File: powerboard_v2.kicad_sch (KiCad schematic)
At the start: 0 parts

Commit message: 信号制御部の回路図の作成 駆動部への信号は変更する可能性あり
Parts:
- added C1, C10, C2, C3, C4, C5, C6, C7, C9: 0.1uf, symbol Device:C
- added C11, C8: 4.7uf, symbol Device:C
- added D1, D2: D_Shockley, symbol Device:D_Shockley
- added J1, J2, J3: Conn_01x02_Pin, symbol Connector:Conn_01x02_Pin
- added J7: Conn_01x04_Socket, symbol Connector:Conn_01x04_Socket
- added J8: Conn_ST_STDC14, symbol Connector:Conn_ST_STDC14
- added R1: 120, symbol Device:R
- added SW1: SW_Wuerth_450301014042, Button_Switch_THT:SW_Slide-03_Wuerth-WS-SLTV_10x2.5x6.4_P2.54mm, symbol Switch:SW_Wuerth_450301014042
- added SW2: SW_Push, symbol Switch:SW_Push
- added U1: STM32F303K8Tx, Package_QFP:LQFP-32_7x7mm_P0.8mm, symbol MCU_ST_STM32F3:STM32F303K8Tx
- added U2: BD33FC0FP, Package_TO_SOT_SMD:TO-252-2, symbol Regulator_Linear:BD33FC0FP
- added U3: MCP2562-E-P, Package_DIP:DIP-8_W7.62mm, symbol Interface_CAN_LIN:MCP2562-E-P
- added U4: BD50FC0FP, Package_TO_SOT_SMD:TO-252-2, symbol Regulator_Linear:BD50FC0FP
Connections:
- new net: C2.2, U1.1 (VDD)
- new net: C1.2, U1.17 (VDD)
- new net: R1.1, SW1.3 (A)
- new net: C5.1, SW2.2, U1.4 (NRST)
- new net: J1.2 (Pin_2), J2.1 (Pin_1)
- new net +24V: J1.1 (Pin_1)
- new net +3.3V: C1.1, C2.1, C4.1, C6.1, C8.2, D1.2 (A), J8.3 (VCC), U2.3 (VO), U3.5 (Vio)
- new net +5V: C10.1, C11.2, C3.1, D2.2 (A), U3.3 (VDD), U4.3 (VO)
- new net +7.5V: C7.1, C9.1, D1.1 (K), D2.1 (K), J3.1 (Pin_1), J7.1 (Pin_1), U2.1 (VCC), U4.1 (VCC)
- new net GND: C5.2, J2.2 (Pin_2), SW2.1, U1.16 (VSS), U1.32 (VSS)
- new net GND1: C10.2, C11.1, C3.2, C4.2, C6.2, C7.2, C8.1, C9.2, J3.2 (Pin_2), J7.2 (Pin_2), J8.5 (GND), J8.7 (GND), SW1.2 (C), U2.2 (GND), U3.2 (VSS), U3.8 (STBY), U4.2 (GND)
- new net can1_rx: U1.21 (PA11), U3.4 (RXD)
- new net can1_tx: U1.22 (PA12), U3.1 (TXD)
- new net can_h: J7.4 (Pin_4), R1.2, U3.7 (CANH)
- new net can_l: J7.3 (Pin_3), SW1.1 (B), U3.6 (CANL)
- new net output-gnd: J8.11 (GNDDetect)
- new net strx: J8.13 (VCP_RX), U1.26 (PB3)
- new net sttx: J8.14 (VCP_TX), U1.27 (PB4)
- new net swclk: J8.6 (JCLK/SWCLK), U1.24 (PA14)
- new net swdio: J8.4 (JTMS/SWDIO), U1.23 (PA13)
- new net デジタル-駆動間信号: U1.10 (PA4)
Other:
- note added: "マイコン用電源"
- note added: "駆動用電源"

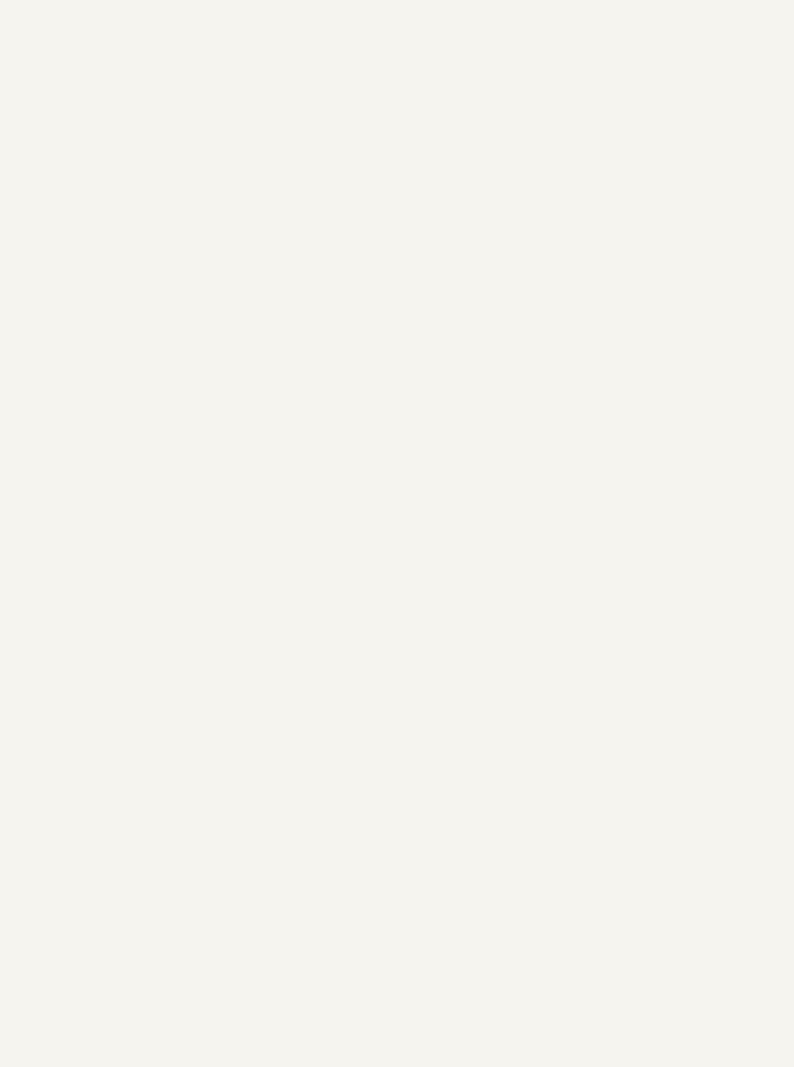
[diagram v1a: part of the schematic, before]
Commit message: リレーの外部ライブラリのインポート
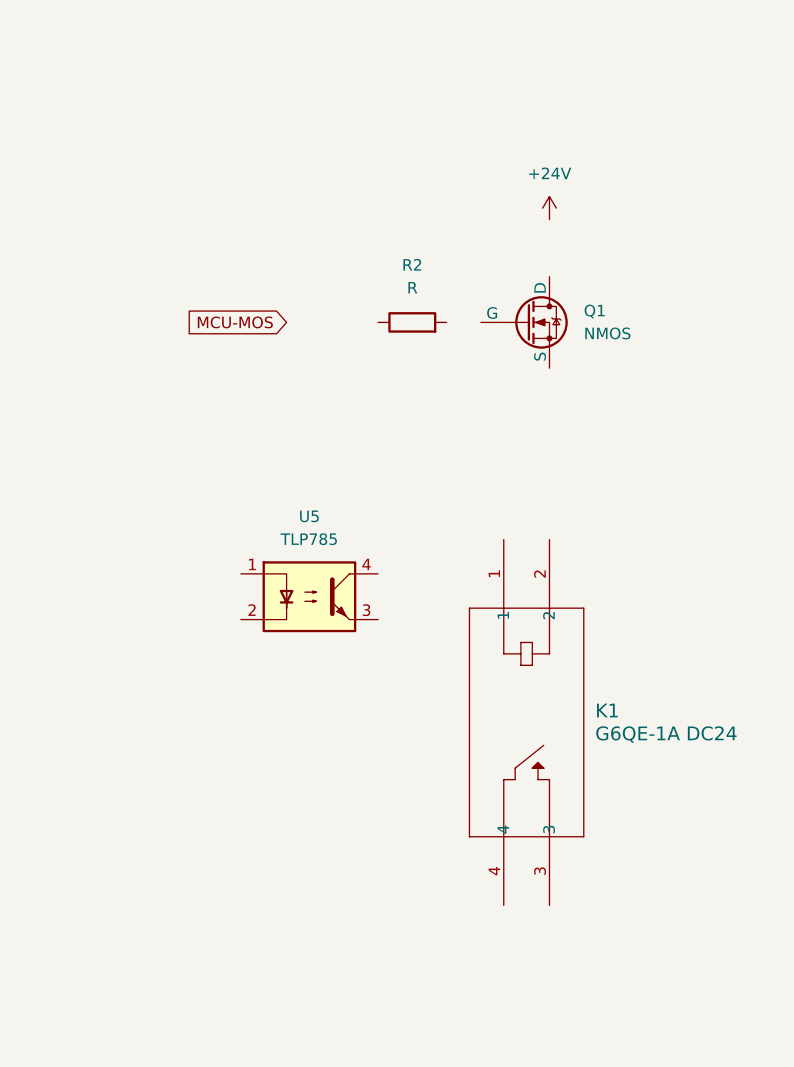
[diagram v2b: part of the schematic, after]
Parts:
- added K1: G6QE-1A DC24, footprints:RELAY_G6QE-1A_OMR, symbol 2026-04-11_13-59-38:G6QE-1A_DC24
- added Q1: NMOS, symbol Simulation_SPICE:NMOS
- added R2: R, symbol Device:R
- added U5: TLP785, Package_DIP:DIP-4_W7.62mm, symbol Isolator:TLP785

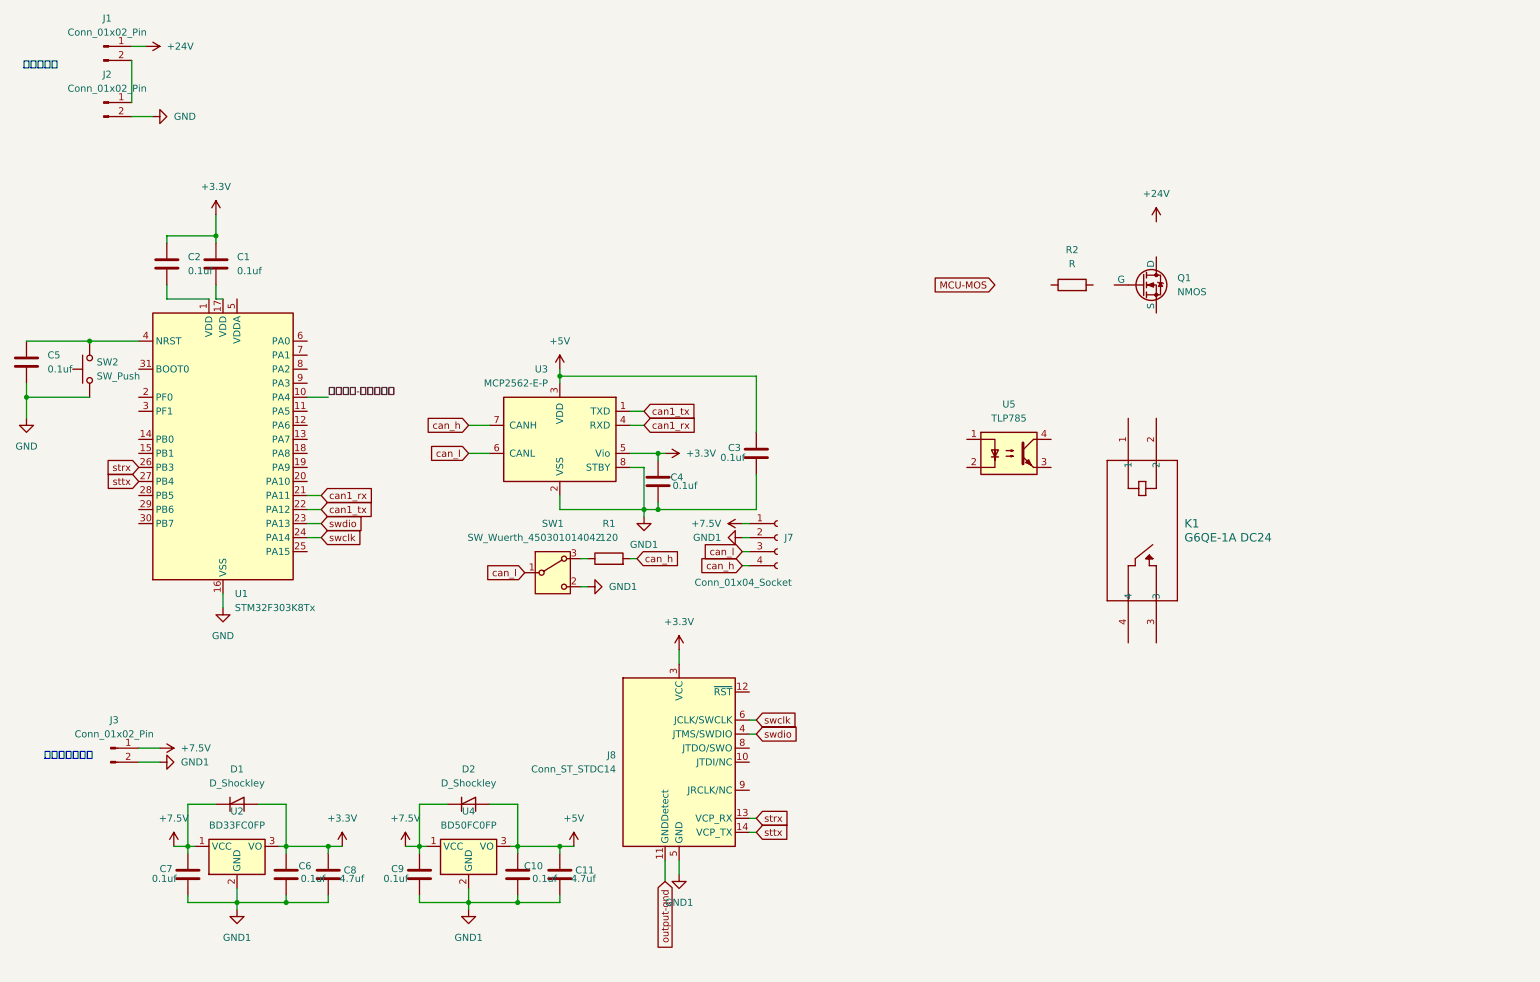
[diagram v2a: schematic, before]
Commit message: 必要部品の配置(フォトカプラ再選定の必要性ありかも？)
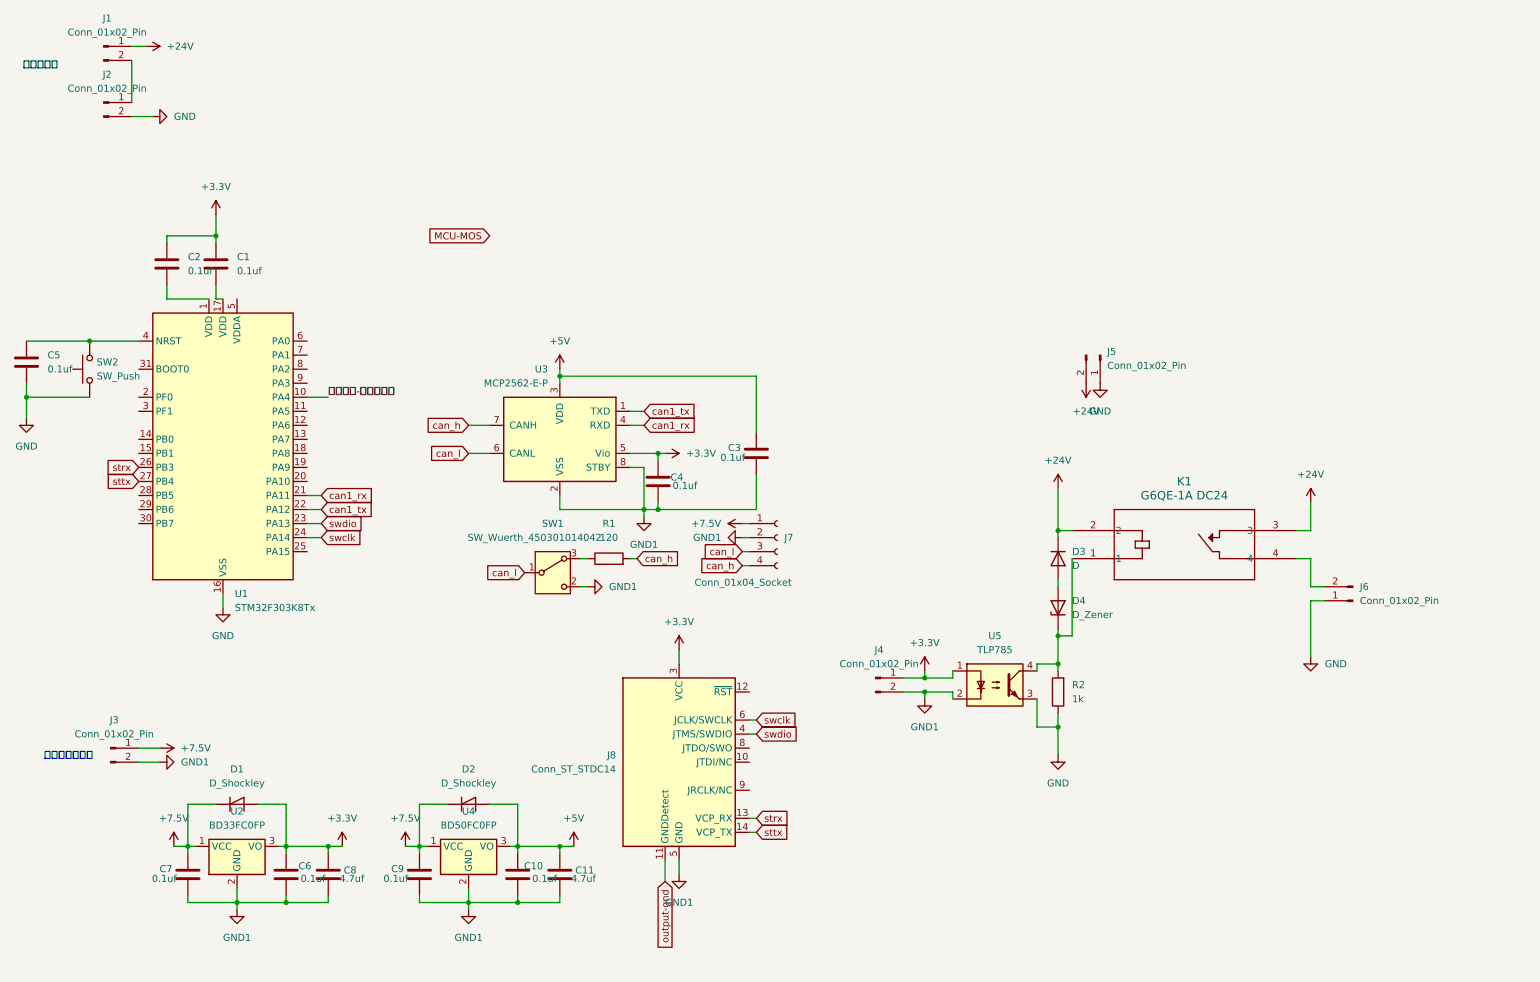
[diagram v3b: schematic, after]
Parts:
- removed Q1: NMOS, symbol Simulation_SPICE:NMOS
- added D3: D, symbol Device:D
- added D4: D_Zener, symbol Device:D_Zener
- added J4, J5, J6: Conn_01x02_Pin, symbol Connector:Conn_01x02_Pin
- R2: value R -> 1k
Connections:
- net +24V: now also K1.2, K1.3, D3.1 (K), J5.2 (Pin_2)
- net +3.3V: now also U5.1, J4.1 (Pin_1)
- net GND: now also R2.1, U5.3, J5.1 (Pin_1), J6.1 (Pin_1)
- net GND1: now also U5.2, J4.2 (Pin_2)
- net at U5.4: now also K1.1, R2.2, D4.1 (K)
- net at K1.4: now also J6.2 (Pin_2)
- new net: D3.2 (A), D4.2 (A)
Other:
- moved on the sheet: K1, R2, U5

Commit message: フォトカプラの置き換えとコンデンサと放電回路の作成(未完了)
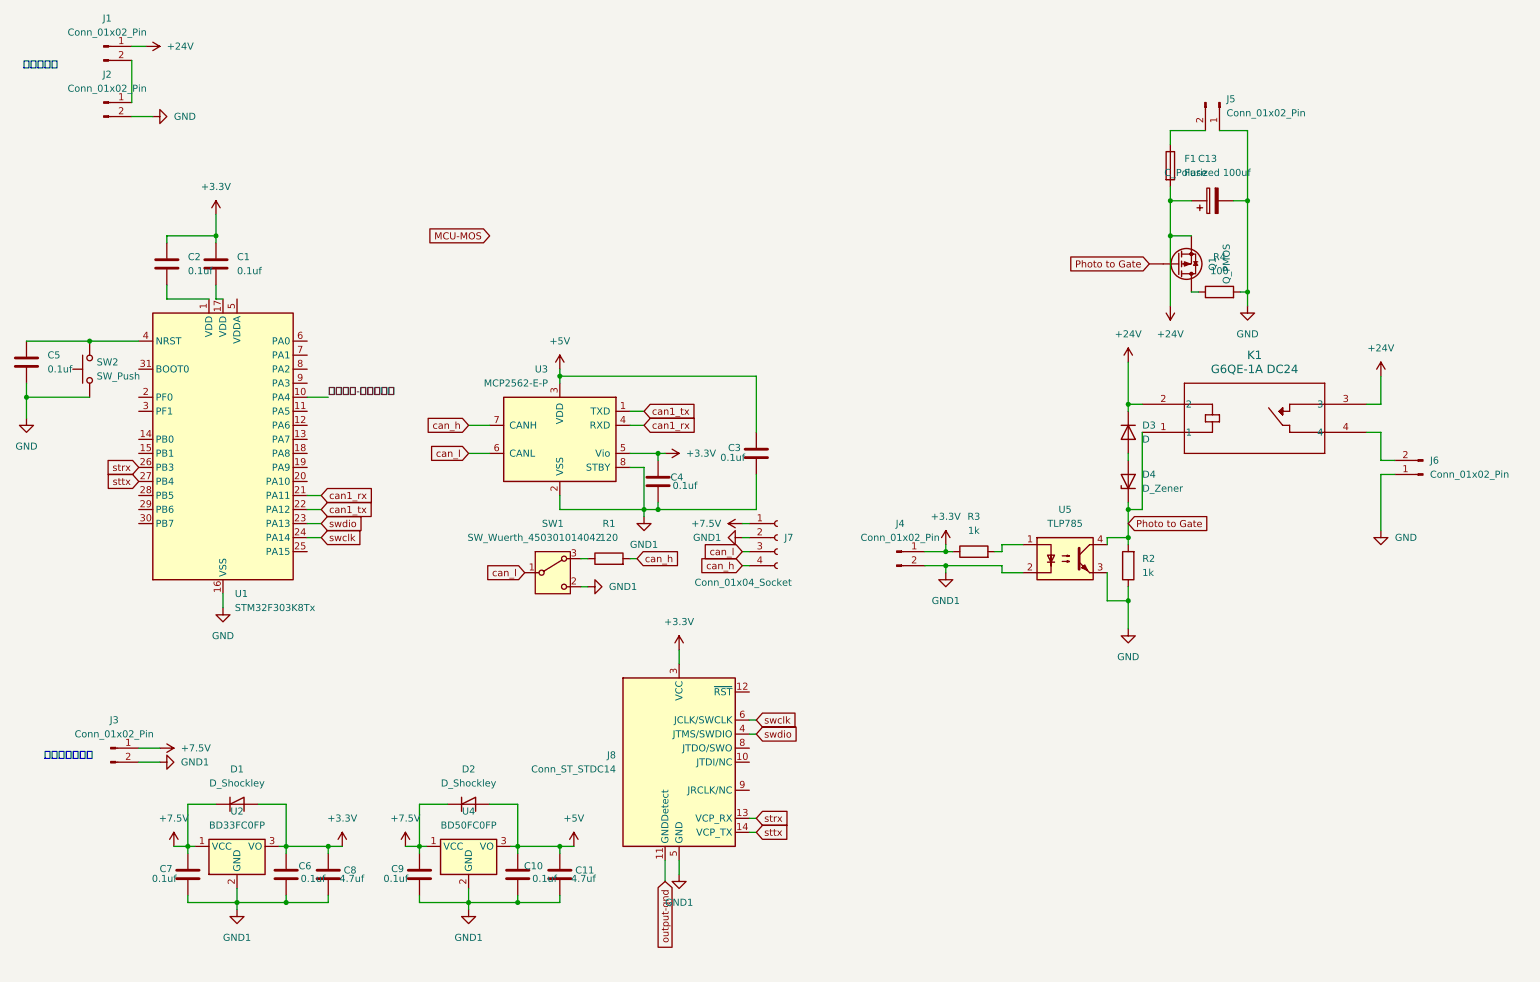
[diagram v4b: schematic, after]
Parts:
- added C13: C_Polarized 100uf, symbol Device:C_Polarized
- added F1: Fuse, symbol Device:Fuse
- added Q1: Q_PMOS, symbol Device:Q_PMOS
- added R3: 1k, symbol Device:R
- added R4: 100, symbol Device:R
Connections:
- net +24V: now also C13.1, F1.2, Q1.S; no longer J5.2 (Pin_2)
- net +3.3V: now also R3.1; no longer U5.1
- net GND: now also C13.2, R4.2
- net Photo to Gate: now reaches D4.1 (K), K1.1, R2.2, U5.4
- net Photo to Gate: now also Q1.G
- new net: R3.2, U5.1
- new net: F1.1, J5.2 (Pin_2)
- new net: Q1.D, R4.1
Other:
- moved on the sheet: D3, D4, J4, J5, J6, K1, R2, U5

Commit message: マイコン制御部を削除
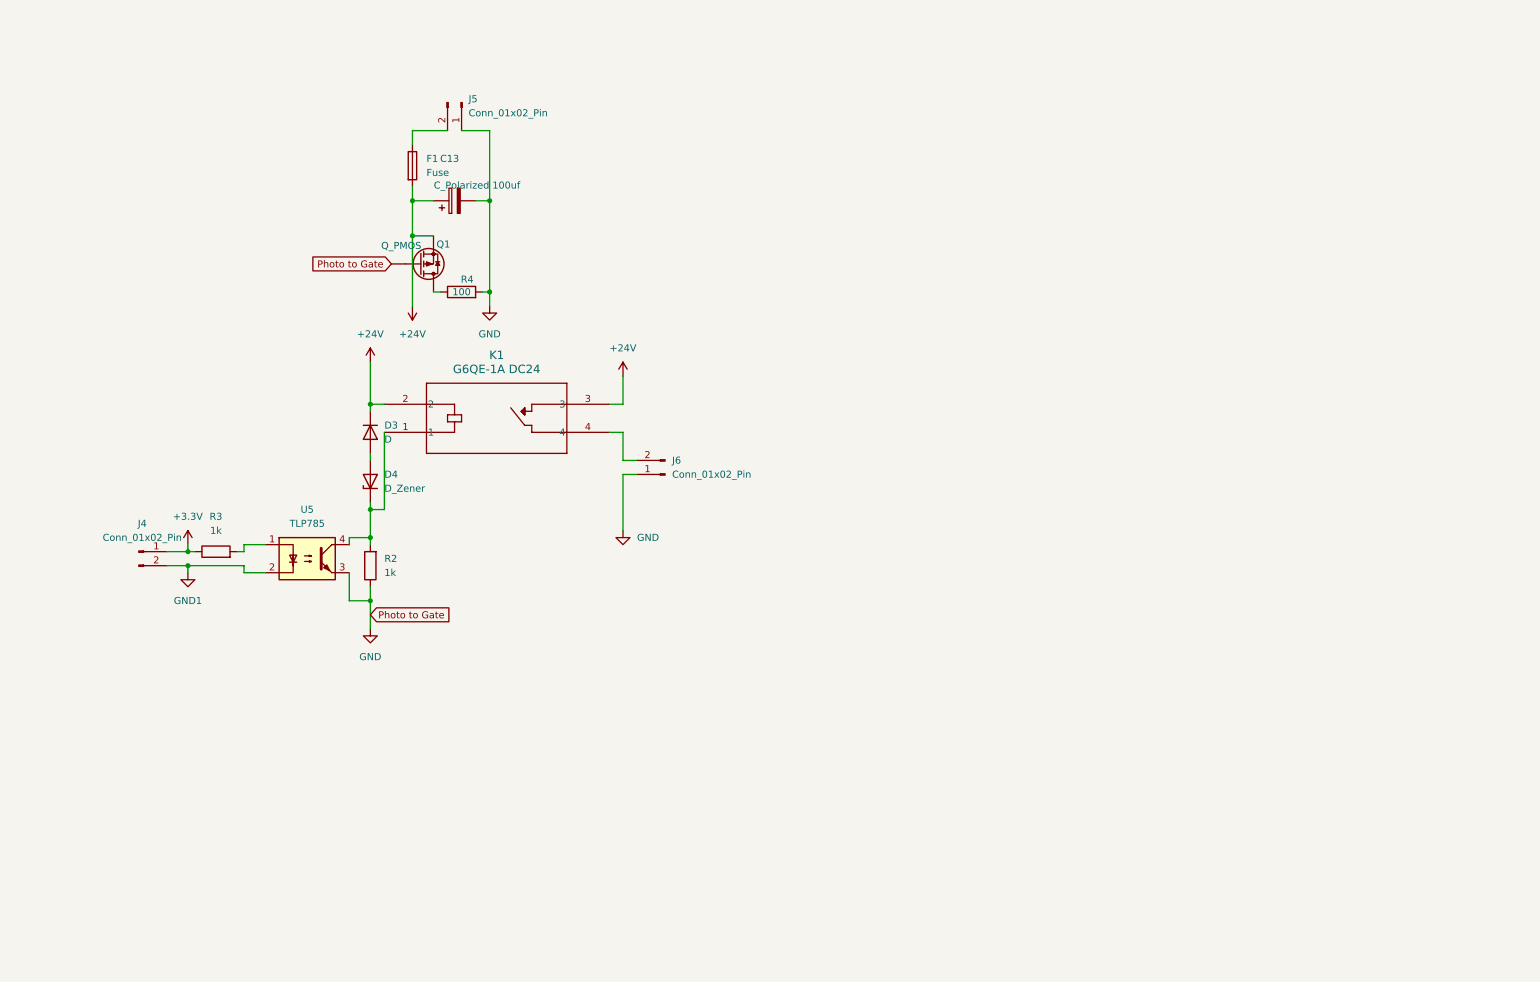
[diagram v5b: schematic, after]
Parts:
- removed C1, C10, C2, C3, C4, C5, C6, C7, C9: 0.1uf, symbol Device:C
- removed C11, C8: 4.7uf, symbol Device:C
- removed D1, D2: D_Shockley, symbol Device:D_Shockley
- removed J1, J2, J3: Conn_01x02_Pin, symbol Connector:Conn_01x02_Pin
- removed J7: Conn_01x04_Socket, symbol Connector:Conn_01x04_Socket
- removed J8: Conn_ST_STDC14, symbol Connector:Conn_ST_STDC14
- removed R1: 120, symbol Device:R
- removed SW1: SW_Wuerth_450301014042, Button_Switch_THT:SW_Slide-03_Wuerth-WS-SLTV_10x2.5x6.4_P2.54mm, symbol Switch:SW_Wuerth_450301014042
- removed SW2: SW_Push, symbol Switch:SW_Push
- removed U1: STM32F303K8Tx, Package_QFP:LQFP-32_7x7mm_P0.8mm, symbol MCU_ST_STM32F3:STM32F303K8Tx
- removed U2: BD33FC0FP, Package_TO_SOT_SMD:TO-252-2, symbol Regulator_Linear:BD33FC0FP
- removed U3: MCP2562-E-P, Package_DIP:DIP-8_W7.62mm, symbol Interface_CAN_LIN:MCP2562-E-P
- removed U4: BD50FC0FP, Package_TO_SOT_SMD:TO-252-2, symbol Regulator_Linear:BD50FC0FP
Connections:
- net GND: now also Q1.G
- net Photo to Gate: no longer names the net of D4.1 (K), K1.1, R2.2, U5.4
- net Photo to Gate: no longer Q1.G
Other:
- note removed: "マイコン用電源"
- note removed: "駆動用電源"
- moved on the sheet: C13, D3, D4, F1, J4, J5, J6, K1, Q1, R2, R3, R4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
